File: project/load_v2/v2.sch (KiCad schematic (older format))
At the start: 105 parts, among them IC1 ATMEGA328-P, P1 CONN_01X02, P10 relay, P2 NGUON, P3 SAC, P4 12N60C, P5 CONN_01X02, P6 button, P7 UART, P8 FAN, P9 7-seg, Q1 Q_NPN_BCE, Q2 Q_NPN_BCE, Q3 Q_NPN_BCE, SW1 reset, U1 LM7812, U2 7805, U3 ICL7660, U4 TL431, U5 LM324N, U6 LM324N, U7 LM7812, Y1 16MHz

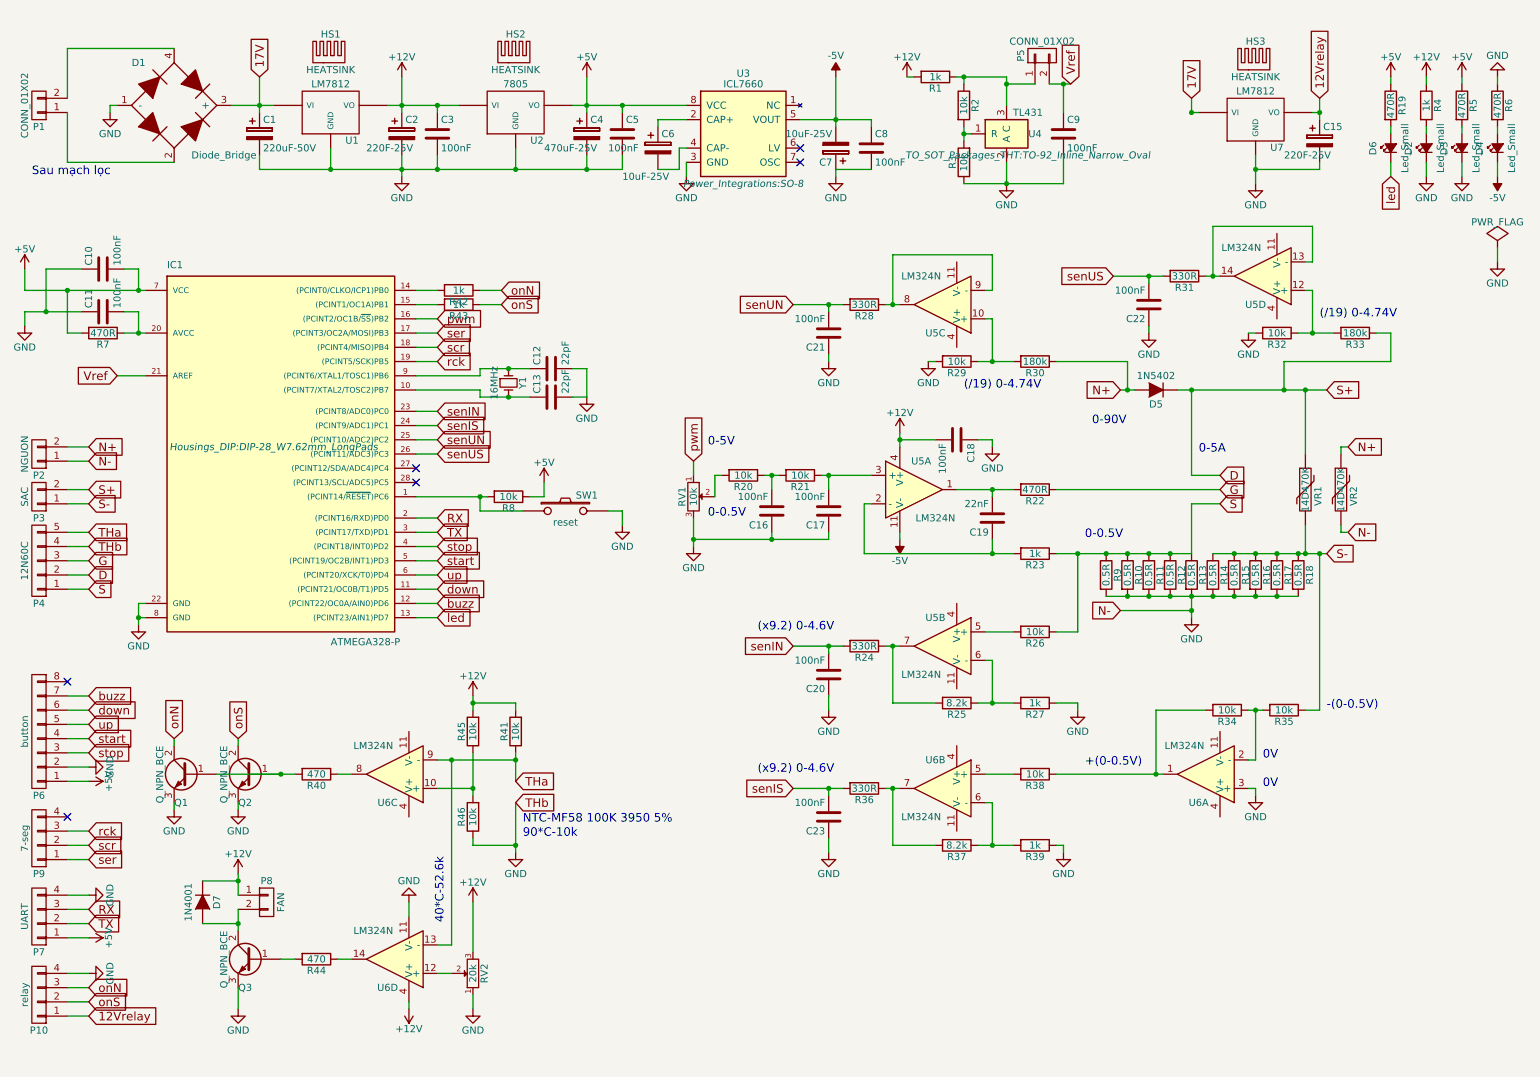
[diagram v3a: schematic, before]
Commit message: schema_load_v2
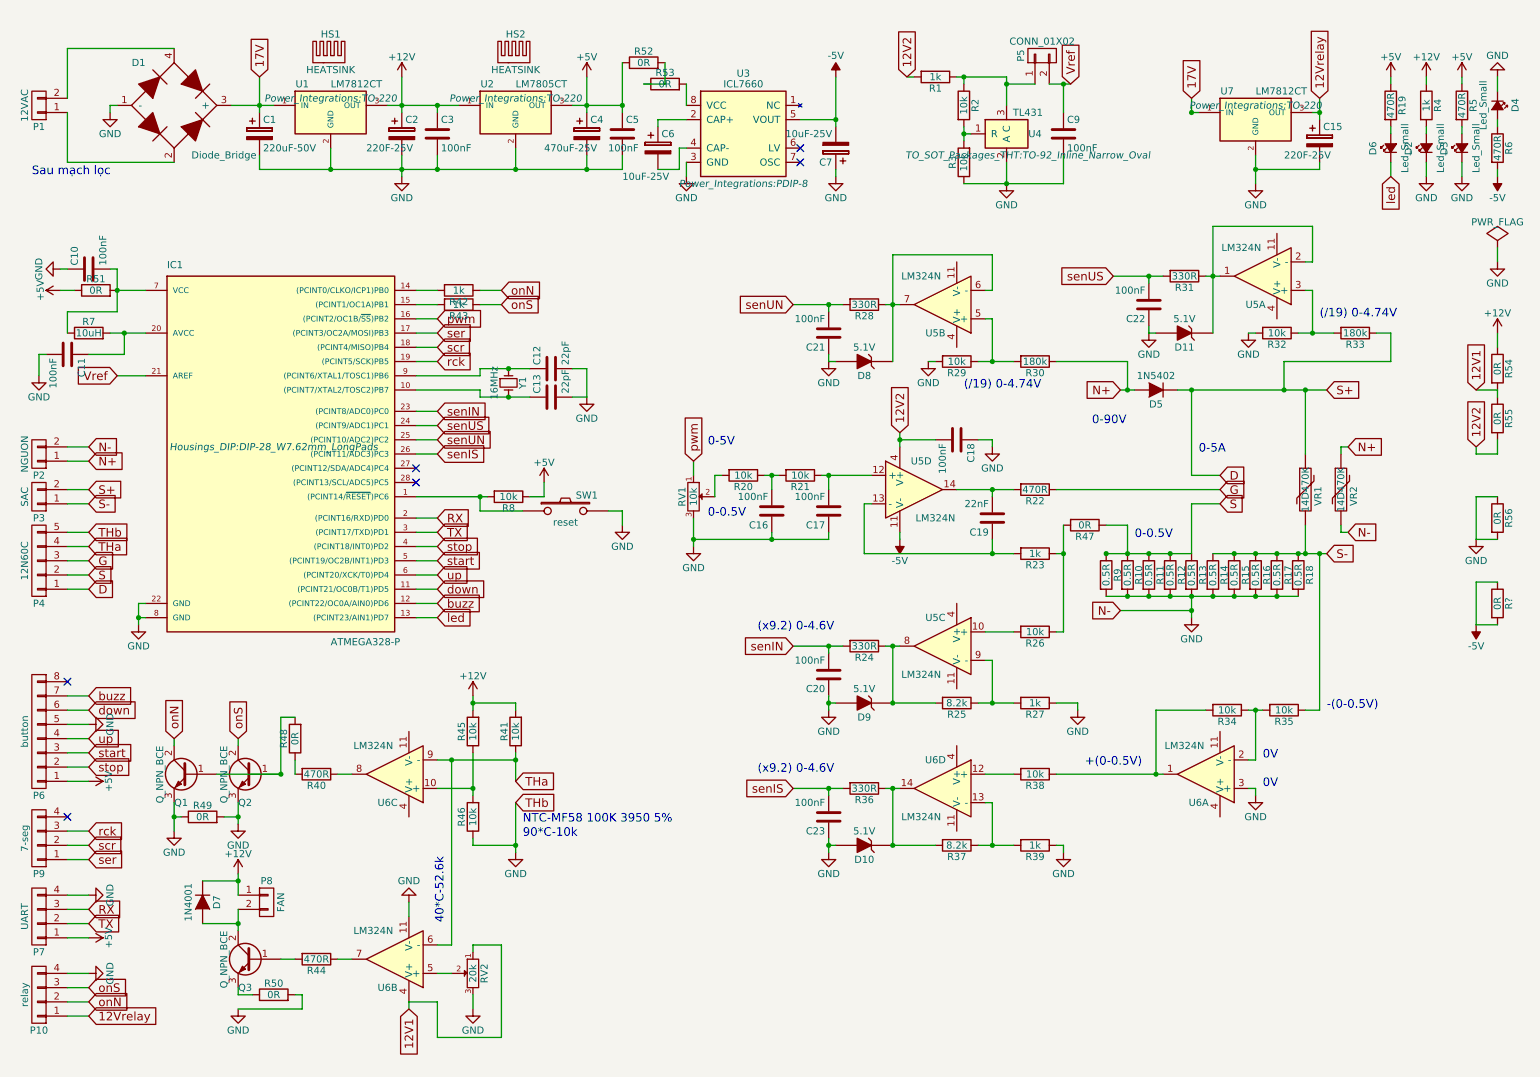
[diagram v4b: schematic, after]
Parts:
- removed C8: 100nF, symbol C
- removed HS3: HEATSINK, symbol HEATSINK
- removed U1, U7: LM7812, symbol LM7812
- removed U2: 7805, symbol 7805
- added D10, D11, D8, D9: 5.1V, Diodes_THT:Diode_DO-35_SOD27_Horizontal_RM10, symbol ZENER
- added R47, R48, R49, R50, R51, R52, R53, R54, R55, R56, R?: 0R, Wire_Connections_Bridges:WireConnection_0.80mmDrill, symbol R
- added U1, U7: LM7812CT, Power_Integrations:TO-220, symbol LM7812CT
- added U2: LM7805CT, Power_Integrations:TO-220, symbol LM7805CT
- C1, C15, C2, C4, C6, C7: footprint (none) -> Capacitors_THT:C_Radial_D5_L6_P2.5
- C10, C12, C13, C9: footprint (none) -> Capacitors_SMD:C_0805_HandSoldering
- C11: footprint (none) -> Capacitors_THT:C_Rect_L7_W2.5_P5
- C16, C17, C19, C20, C21, C22, C23, C3, C5: footprint (none) -> Capacitors_THT:C_Disc_D3_P2.5
- C18: footprint (none) -> Capacitors_THT:C_Rect_L7_W2_P5
- D1: footprint (none) -> Diodes_THT:Diode_Bridge_18.5x5.5
- D2, D3, D4, D6: footprint (none) -> LEDs:LED-3MM
- D5: footprint (none) -> Diodes_THT:Diode_DO-201AD_Horizontal_RM15
- D7: footprint (none) -> Diodes_THT:Diode_DO-35_SOD27_Horizontal_RM10
- HS1, HS2: footprint (none) -> Heatsinks:Heatsink_Stonecold_HS-132_32x14mm_2xFixation1.5mm
- P1: value CONN_01X02 -> 12VAC; footprint (none) -> Connectors_Phoenix:PhoenixContact_MCV-G_02x5.08mm_Vertical
- P10, P9: footprint (none) -> Connectors:XH2.54-4P
- P2, P3: footprint (none) -> Connectors_Phoenix:PhoenixContact_MCV-G_02x5.08mm_Vertical
- P4: footprint (none) -> Connectors_Phoenix:PhoenixContact_MCV-G_05x5.08mm_Vertical
- P5: footprint (none) -> Pin_Headers:Pin_Header_Straight_1x02
- P6: footprint Socket_Strips:Socket_Strip_Straight_1x08 -> Connectors:XH2.54-8P
- P7: footprint (none) -> Pin_Headers:Pin_Header_Straight_1x04
- P8: footprint (none) -> Connectors:XH2.54-2P
- Q1, Q2, Q3: footprint (none) -> TO_SOT_Packages_THT:TO-92_Inline_Narrow_Oval
- R1, R19, R20, R21, R22, R23, R24, R25, R26, R27, R28, R31, R32, R33, R34, R35, R36, R37, R38, R39, R4, R41, R42, R43, R45, R46, R5, R6, R8: footprint (none) -> Resistors_THT:Resistor_Horizontal_RM7mm
- R10, R11, R12, R13, R14, R15, R16, R17, R18, R9: footprint (none) -> Resistors_SMD:R_2512_HandSoldering
- R2, R3: footprint (none) -> Resistors_SMD:R_0805_HandSoldering
- R29, R30: footprint (none) -> Resistors_THT:Resistor_Horizontal_RM15mm
- R40, R44: value 470 -> 470R; footprint (none) -> Resistors_THT:Resistor_Horizontal_RM7mm
- R7: value 470R -> 10uH; footprint (none) -> Resistors_THT:Resistor_Horizontal_RM7mm
- RV1, RV2: footprint (none) -> Potentiometers:Potentiometer_Bourns_3296W_3-8Zoll_Inline_ScrewUp
- SW1: footprint (none) -> Buttons_Switches_THT:SW_PUSH_6mm
- U3: footprint Power_Integrations:SO-8 -> Power_Integrations:PDIP-8
- U5, U6: footprint (none) -> Housings_DIP:DIP-14_W7.62mm_LongPads
- VR1, VR2: footprint (none) -> Varistors:RV_Disc_D15.5_W3.9_P7.5
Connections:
- net +12V: now also R54.1, U1.3 (OUT), U2.1 (IN); no longer C18.2, R1.2, RV2.3, U5.4 (V+), U6.4 (V+)
- net +5V: now also R51.1, R52.1, U2.3 (OUT); no longer C10.2, IC1.7 (VCC), R7.2, U3.8 (VCC)
- net -5V: now also R6.2, R?.1, R?.2; no longer D4.1 (K)
- net 12Vrelay: now also U7.3 (OUT)
- net 17V: now also U1.1 (IN), U7.1 (IN)
- net D: now also P4.1 (P1); no longer P4.2 (P2)
- net GND: now also C11.2, D4.1 (K), P2.2 (P2), P4.5 (P5), P6.5 (P5), RV2.3, D10.2 (A), D11.2 (A), D8.2 (A), D9.2 (A), R49.1, R49.2, R50.2, R56.1, R56.2, U1.2 (GND), U2.2 (GND), U7.2 (GND); no longer C11.1, P2.1 (P1), P4.4 (P4), P6.2 (P2), Q3.3 (E), R6.1, RV2.1
- net N+: now also P2.1 (P1); no longer P2.2 (P2)
- net S: now also P4.2 (P2), R47.1; no longer P4.1 (P1), R23.1, R26.1
- net THa: now also P4.4 (P4), U6.6 (-); no longer P4.5 (P5), U6.13 (-)
- net onN: now also P10.2 (P2); no longer P10.3 (P3)
- net onS: now also P10.3 (P3); no longer P10.2 (P2)
- net senIS: now also IC1.26 ((PCINT11/ADC3)PC3); no longer IC1.24 ((PCINT9/ADC1)PC1)
- net senUS: now also IC1.24 ((PCINT9/ADC1)PC1); no longer IC1.26 ((PCINT11/ADC3)PC3)
- net start: now also P6.3 (P3); no longer P6.4 (P4)
- net stop: now also P6.2 (P2); no longer P6.3 (P3)
- net up: now also P6.4 (P4); no longer P6.5 (P5)
- net at D4.2 (A): now also R6.1; no longer R6.2
- net at C19.2, R22.2: now also U5.14; no longer U5.1
- net at C19.1, R23.2: now also U5.13 (-); no longer U5.2 (-)
- net at C17.2, R21.1: now also U5.12 (+); no longer U5.3 (+)
- net at R26.2: now also U5.10 (+); no longer U5.5 (+)
- net at R25.1, R27.2: now also U5.9 (-); no longer U5.6 (-)
- net at R24.1, R25.2: now also U5.8, D9.1 (K); no longer U5.7
- net at R29.1, R30.2: now also U5.5 (+); no longer U5.10 (+)
- net at R32.1, R33.2: now also U5.3 (+); no longer U5.12 (+)
- net at R38.2: now also U6.12 (+); no longer U6.5 (+)
- net at R37.1, R39.2: now also U6.13 (-); no longer U6.6 (-)
- net at R36.1, R37.2: now also U6.14, D10.1 (K); no longer U6.7
- net at RV2.2: now also U6.5 (+); no longer U6.12 (+)
- net at R44.1: now also U6.7; no longer U6.14
- net at Q1.1 (B), Q2.1 (B): now also R48.2; no longer R40.2
- new net: R53.2, U3.8 (VCC)
- new net: C11.1, IC1.20 (AVCC), R7.2
- new net: C10.2, IC1.7 (VCC), R51.2, R7.1
- new net: D8.1 (K), R28.1, U5.6 (-), U5.7
- new net: D11.1 (K), R31.1, U5.1, U5.2 (-)
- new net: R23.1, R26.1, R47.2
- new net: R40.2, R48.1
- new net: Q3.3 (E), R50.1
- new net: R52.2, R53.1
- new net 12V1: R54.2, R55.1, RV2.1, U6.4 (V+)
- new net 12V2: C18.2, R1.2, R55.2, U5.4 (V+)
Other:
- moved on the sheet: C10, D4, R6

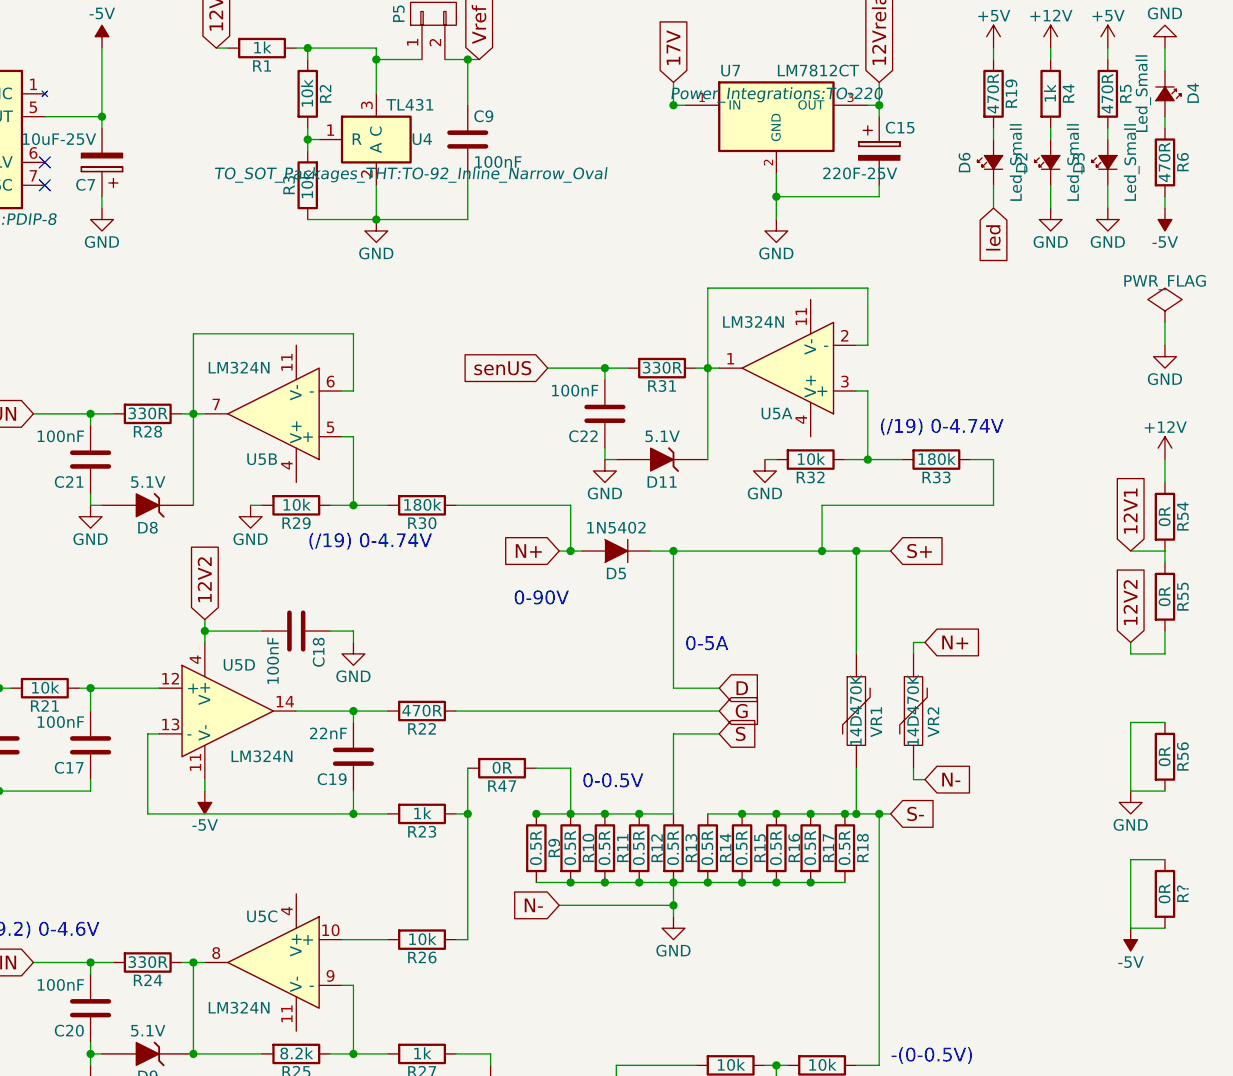
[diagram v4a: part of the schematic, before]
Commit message: schema_load_v2
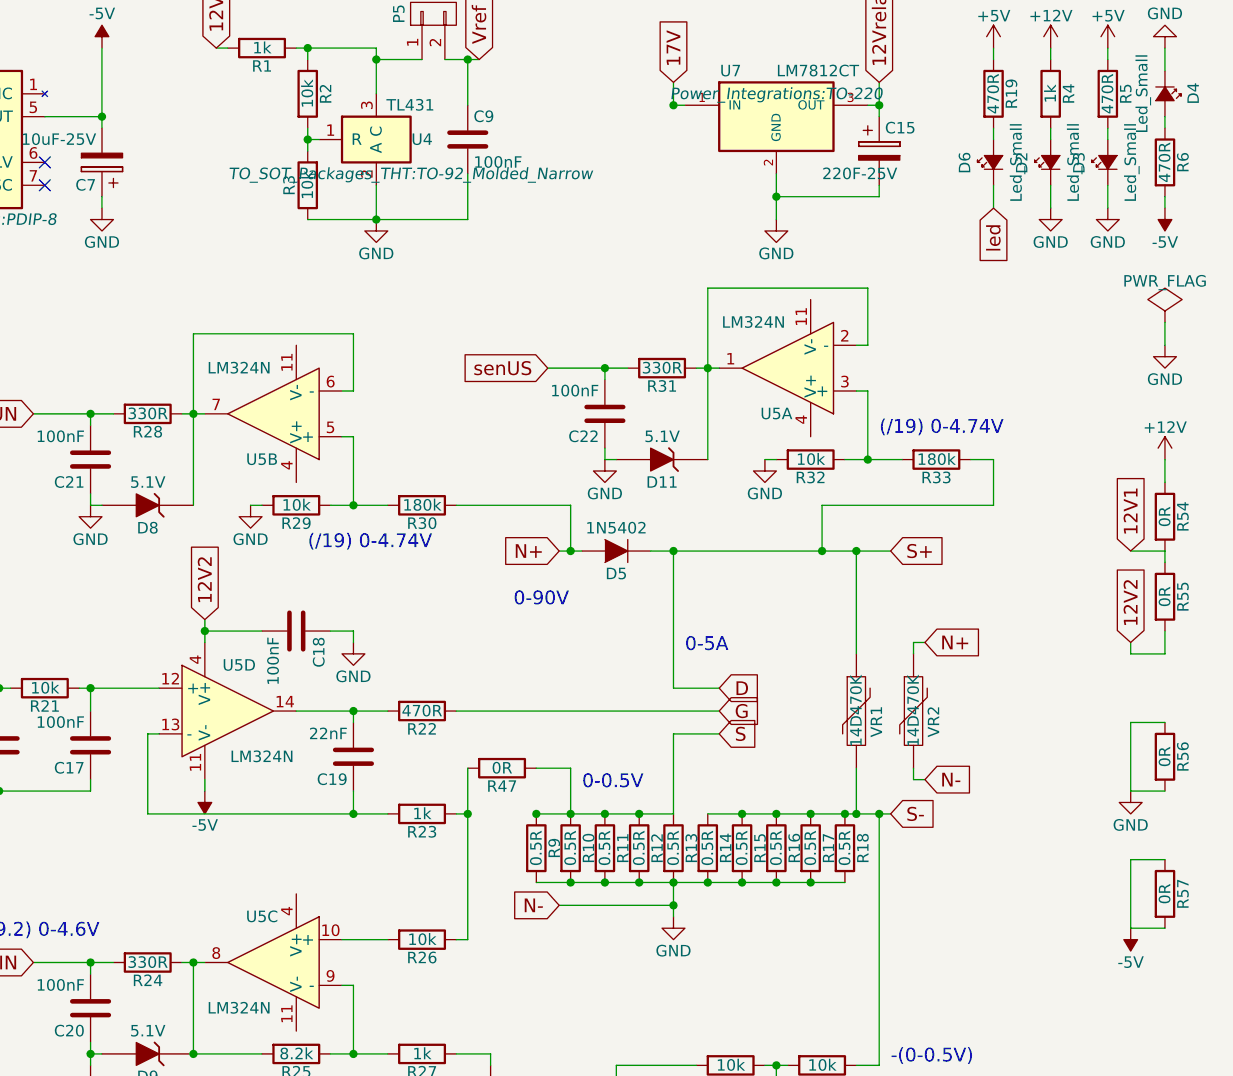
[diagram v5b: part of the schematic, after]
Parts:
- Q1, Q2, Q3, U4: footprint TO_SOT_Packages_THT:TO-92_Inline_Narrow_Oval -> TO_SOT_Packages_THT:TO-92_Molded_Narrow
- gave numbers to parts that had none: 1
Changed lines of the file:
@@
 $EndComp
 $Comp
-L -5V #PWR50
+L -5V #PWR51
 U 1 1 583BE9A9
 P 11000 1500
-F 0 "#PWR50" H 11000 1600 50  0001 C CNN
+F 0 "#PWR51" H 11000 1600 50  0001 C CNN
 F 1 "-5V" H 11000 1650 50  0000 C CNN
 F 2 "" H 11000 1500 50  0000 C CNN
@@
 F 0 "U4" H 7750 1200 50  0000 C CNN
 F 1 "TL431" H 7700 1350 50  0000 C CNN
-F 2 "TO_SOT_Packages_THT:TO-92_Inline_Narrow_Oval" H 7700 1050 50  0000 C CIN
+F 2 "TO_SOT_Packages_THT:TO-92_Molded_Narrow" H 7700 1050 50  0000 C CIN
 F 3 "" H 7550 1200 50  0000 C CNN
 	1    7550 1200
@@
 F 0 "Q2" H 2350 5500 50  0000 R CNN
 F 1 "Q_NPN_BCE" V 2450 5900 50  0000 R CNN
-F 2 "TO_SOT_Packages_THT:TO-92_Inline_Narrow_Oval" H 2450 5800 50  0001 C CNN
+F 2 "TO_SOT_Packages_THT:TO-92_Molded_Narrow" H 2450 5800 50  0001 C CNN
 F 3 "" H 2250 5700 50  0000 C CNN
 	1    2250 5700
@@
 F 0 "Q1" H 1900 5500 50  0000 R CNN
 F 1 "Q_NPN_BCE" V 2000 5900 50  0000 R CNN
-F 2 "TO_SOT_Packages_THT:TO-92_Inline_Narrow_Oval" H 2000 5800 50  0001 C CNN
+F 2 "TO_SOT_Packages_THT:TO-92_Molded_Narrow" H 2000 5800 50  0001 C CNN
 F 3 "" H 1800 5700 50  0000 C CNN
 	1    1800 5700
@@
 F 0 "Q3" H 2350 6800 50  0000 R CNN
 F 1 "Q_NPN_BCE" V 2450 7200 50  0000 R CNN
-F 2 "TO_SOT_Packages_THT:TO-92_Inline_Narrow_Oval" H 2450 7100 50  0001 C CNN
+F 2 "TO_SOT_Packages_THT:TO-92_Molded_Narrow" H 2450 7100 50  0001 C CNN
 F 3 "" H 2250 7000 50  0000 C CNN
 	1    2250 7000
@@
 	10850 3750 10850 4050
 $Comp
-L R R?
+L R R57
 U 1 1 58578314
 P 11000 4500
-F 0 "R?" V 11080 4500 50  0000 C CNN
+F 0 "R57" V 11080 4500 50  0000 C CNN
 F 1 "0R" V 11000 4500 50  0000 C CNN
 F 2 "Wire_Connections_Bridges:WireConnection_0.80mmDrill" V 10930 4500 50  0001 C CNN
@@
 $EndComp
 $Comp
-L -5V #PWR?
+L -5V #PWR49
 U 1 1 5857C3AE
 P 10850 4650
-F 0 "#PWR?" H 10850 4750 50  0001 C CNN
+F 0 "#PWR49" H 10850 4750 50  0001 C CNN
 F 1 "-5V" H 10850 4800 50  0000 C CNN
 F 2 "" H 10850 4650 50  0000 C CNN
